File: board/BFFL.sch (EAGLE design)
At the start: 25 parts, among them IC1 LM317MSTT3, Q1 FDS5680, U1 ATTINY84-20SSU

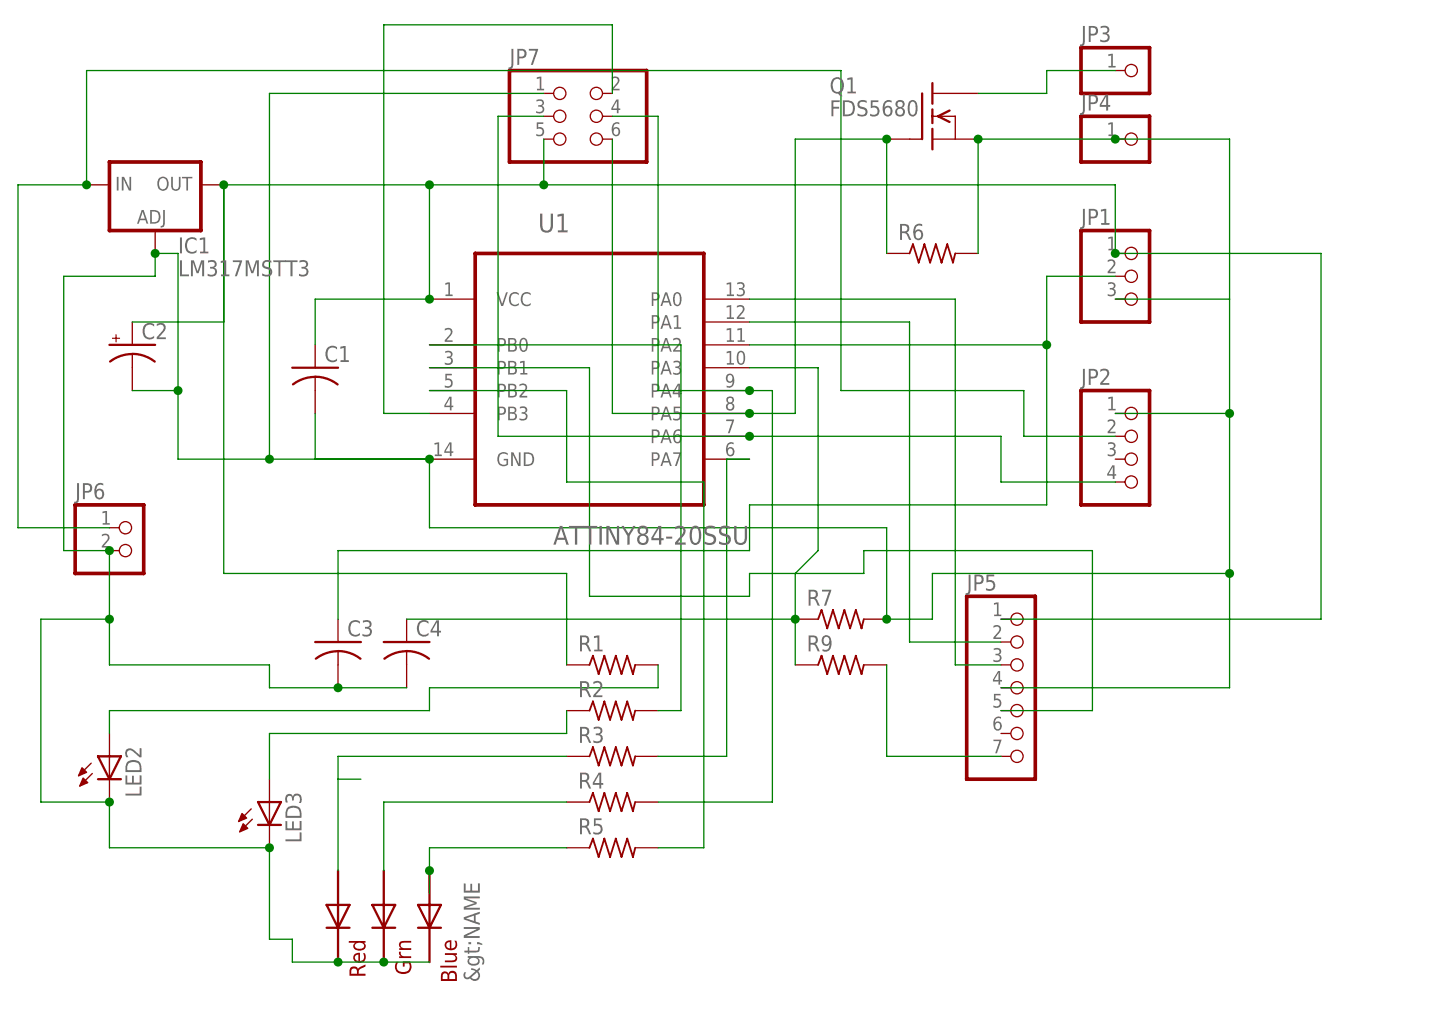
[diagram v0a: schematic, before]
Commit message: Rev B of PCB, preliminary
Corrects multiple faults in Rev A and improves mounting options.
Silkscreen still needs to be done.
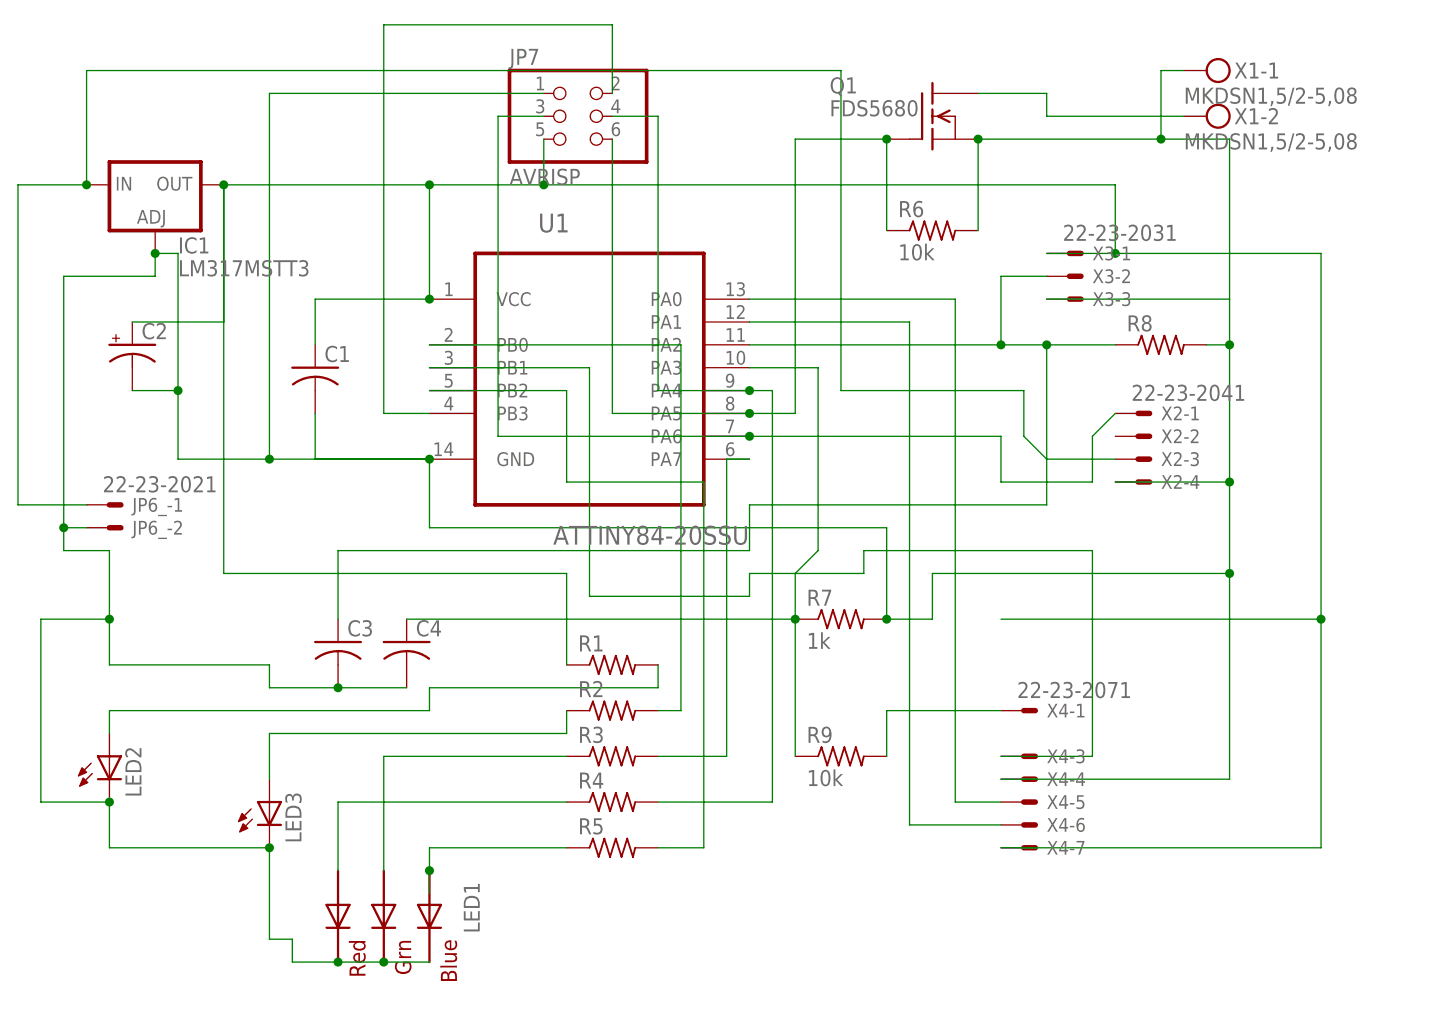
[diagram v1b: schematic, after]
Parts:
- removed JP1: (no value), pinhead:PINHD-1X3
- removed JP2: (no value), pinhead:PINHD-1X4
- removed JP3, JP4: (no value), pinhead:PINHD-1X1
- removed JP5: (no value), pinhead:PINHD-1X7
- removed JP6: (no value), pinhead:PINHD-1X2
- added JP6_: 22-23-2021, con-molex:22-23-2021
- added R8: (no value), rcl:R-US_R1206
- added X1: MKDSN1,5/2-5,08, con-phoenix-508:MKDSN1,5/2-5,08
- added X2: 22-23-2041, con-molex:22-23-2041
- added X3: 22-23-2031, con-molex:22-23-2031
- added X4: 22-23-2071, con-molex:22-23-2071
- JP7: value (none) -> AVRISP
- R6, R9: value (none) -> 10k
- R7: value (none) -> 1k
- renumbered LED4 to LED1
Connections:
- net N$1: now also X4-1.S; no longer JP5.7
- net N$10: now also R3.1; no longer R4.1
- net N$12: now also X1-2.KL; no longer JP3.1
- net N$13: now also JP6_-2.S, R8.2, X1-1.KL, X2-4.S, X3-3.S, X4-4.S; no longer JP1.3, JP2.1, JP4.1, JP5.4, JP6.2
- net N$16: now also X2-1.S; no longer JP2.4
- net N$17: now also X4-3.S; no longer JP5.5
- net N$19: now also R8.1, X3-2.S; no longer JP1.2
- net N$21: now also X4-5.S; no longer JP5.3
- net N$22: now also X4-6.S; no longer JP5.2
- net N$3: now also JP6_-1.S, X2-3.S; no longer JP2.2, JP6.1
- net N$6: now also X3-1.S, X4-7.S; no longer JP1.1, JP5.1
- net N$9: now also R4.1; no longer R3.1
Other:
- moved on the sheet: R6, R9

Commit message: Update board
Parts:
- renumbered IC1 to U2, JP6_ to JP1, JP7 to JP6, X1 to JP3, X2 to JP5, X3 to JP4, X4 to JP2
